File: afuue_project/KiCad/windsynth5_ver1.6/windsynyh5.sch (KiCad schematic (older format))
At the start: 29 parts, among them P1 SENSOR, P2 SPEAKER, P3 HEADPHONE, P4 POWER, P5 EXT, P6 AE-PAM8012, P7 I2C, P8 TRS MIDI, SW1 SW_SPDT, U1 ESP32-DEVKIT-C, U2 L7805

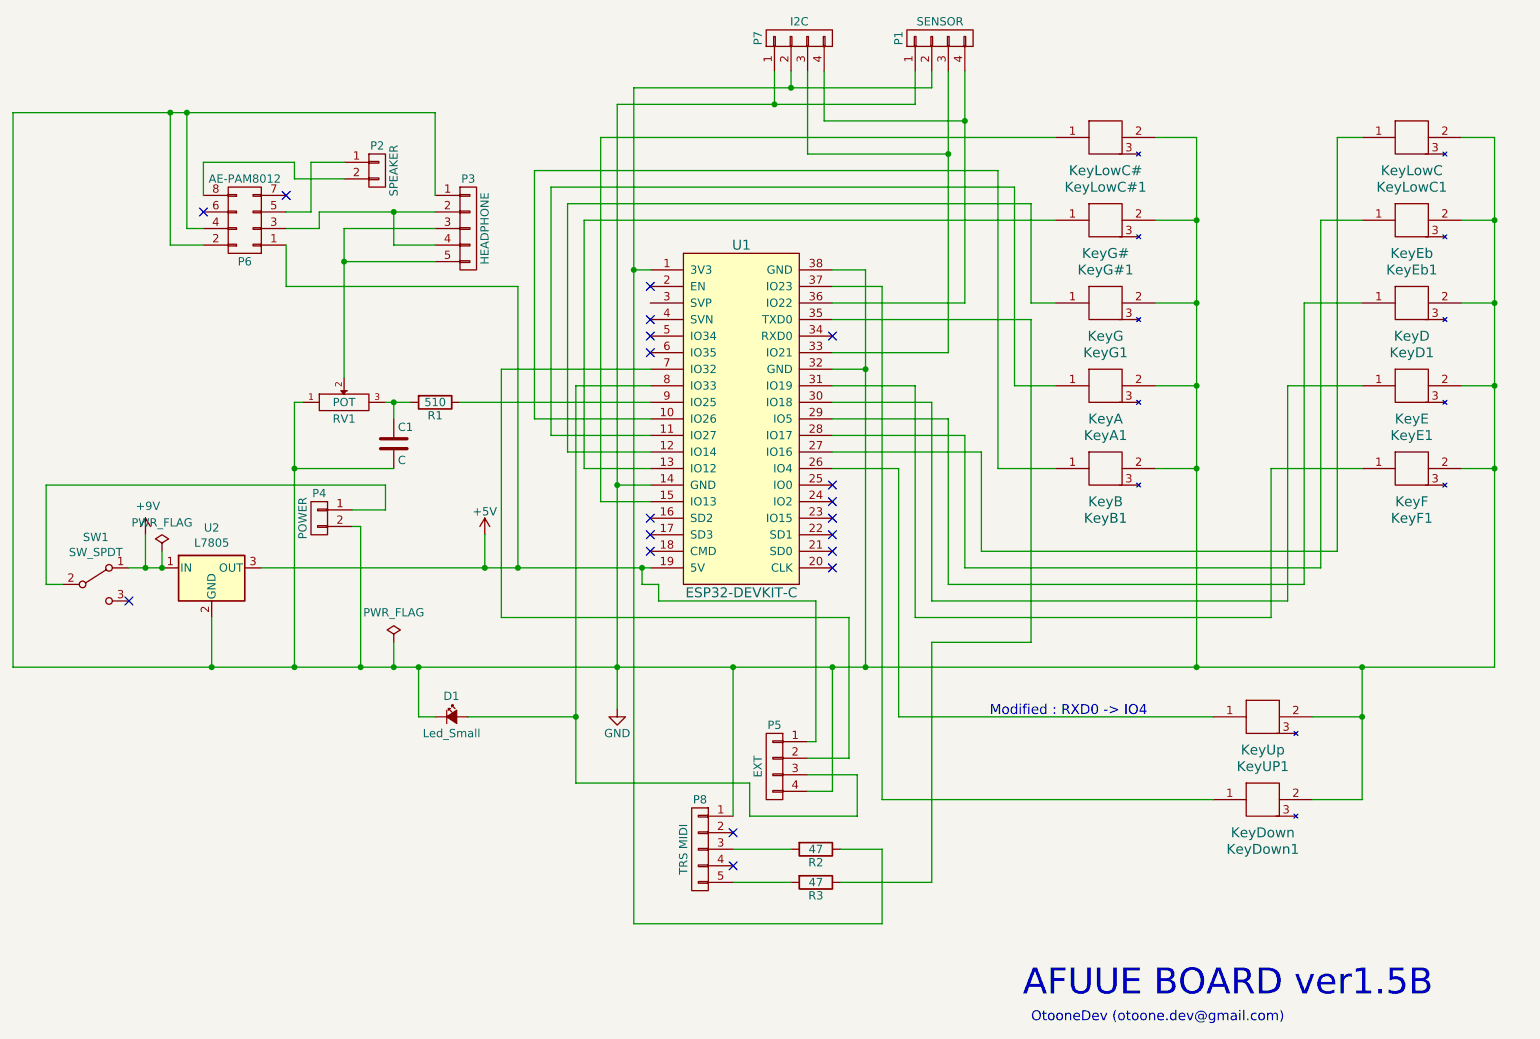
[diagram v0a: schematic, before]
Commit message: 電池内蔵版v06のソースやデータを追加
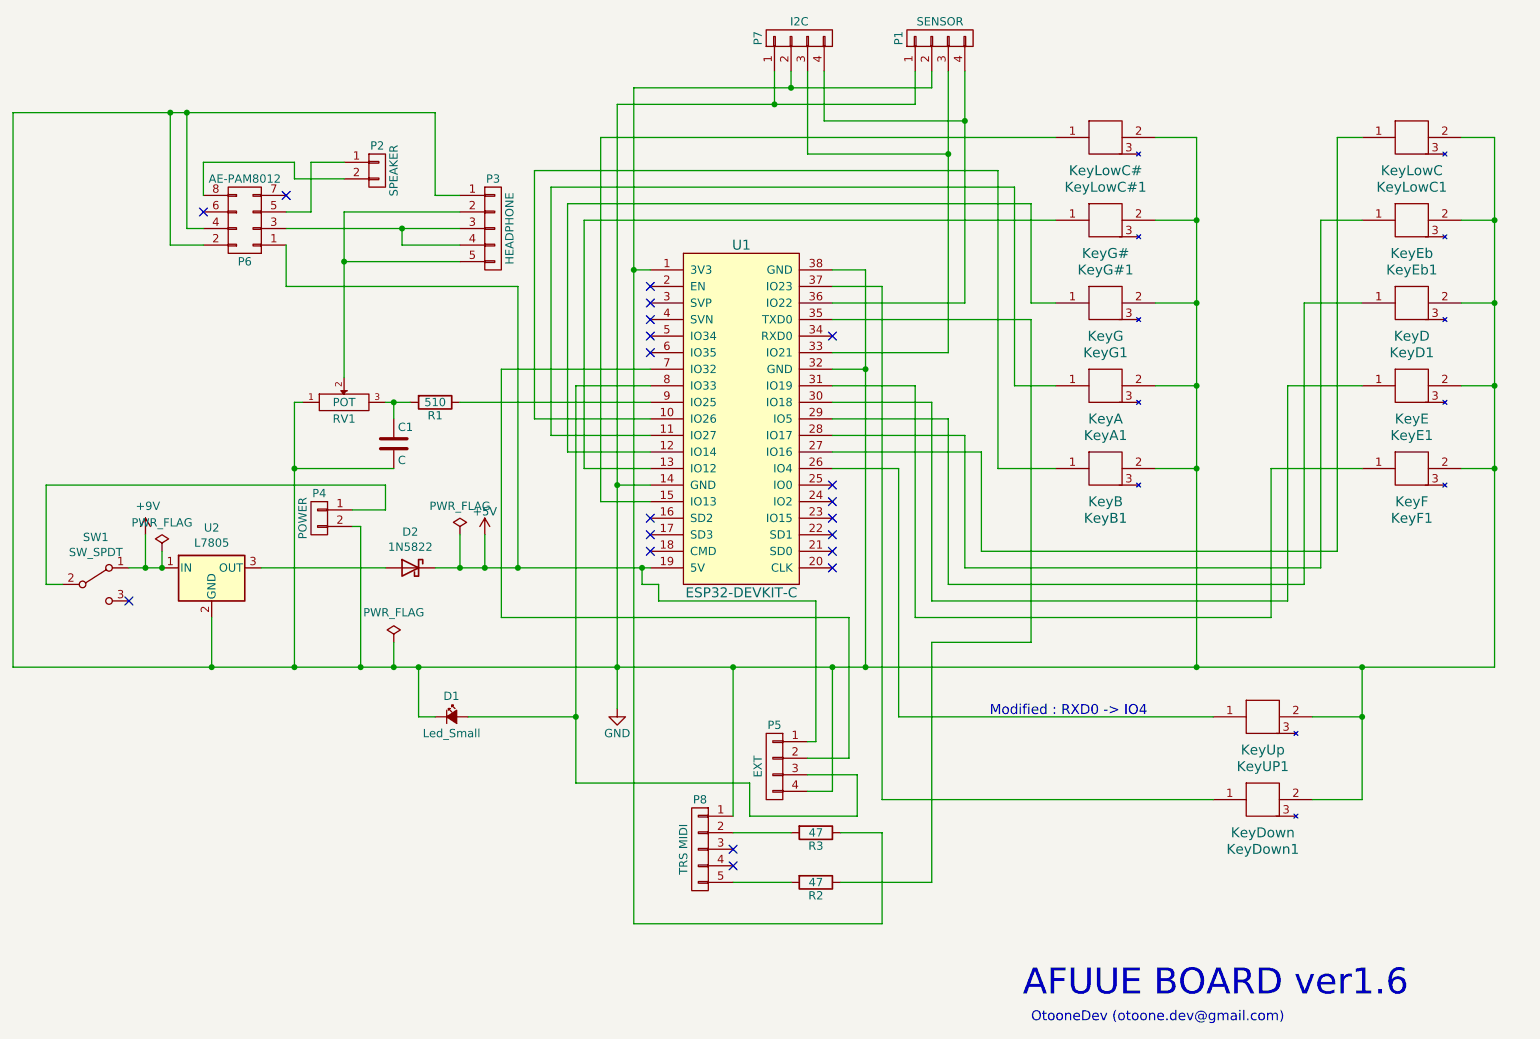
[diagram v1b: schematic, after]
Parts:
- added D2: 1N5822, Connector_PinHeader_2.54mm:PinHeader_1x02_P2.54mm_Vertical, symbol Diode:1N5822
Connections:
- net +5V: now also D2.1 (K); no longer U2.3 (OUT)
- net at P1.2 (P2), P7.2 (P2), U1.1 (3V3): now also R3.1; no longer R2.1
- net at U1.35 (TXD0): now also R2.1; no longer R3.1
- net at P3.5 (P5), RV1.2: now also P3.2 (P2); no longer P3.3 (P3)
- net at P3.4 (P4), P6.3 (P3): now also P3.3 (P3); no longer P3.2 (P2)
- net at P8.2 (P2): now also R3.2
- net at P8.3 (P3): no longer R2.2
- net at P8.5 (P5): now also R2.2; no longer R3.2
- new net: D2.2 (A), U2.3 (OUT)
- no-connect marks 19 -> 20
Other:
- note added: "AFUUE BOARD ver1.6"
- note removed: "AFUUE BOARD ver1.5B"
- moved on the sheet: P3, R2, R3
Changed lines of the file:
@@
 L windsynyh5-rescue:CONN_01X05 P3
 U 1 1 5E29EC6C
-P 3800 2200
-F 0 "P3" H 3800 2500 50  0000 C CNN
-F 1 "HEADPHONE" V 3900 2200 50  0000 C CNN
-F 2 "HPJack_PJ307:PJ-307 AudioJack" H 3800 2200 50  0001 C CNN
-F 3 "" H 3800 2200 50  0000 C CNN
-	1    3800 2200
+P 3950 2200
+F 0 "P3" H 3950 2500 50  0000 C CNN
+F 1 "HEADPHONE" V 4050 2200 50  0000 C CNN
+F 2 "HPJack_PJ307:PJ-307 AudioJack" H 3950 2200 50  0001 C CNN
+F 3 "" H 3950 2200 50  0000 C CNN
+	1    3950 2200
 	1    0    0    -1
 $EndComp
@@
 NoConn ~ 2200 2100
 Text Notes 7150 6850 0    157  ~ 0
-AFUUE BOARD ver1.5B
+AFUUE BOARD ver1.6
 Text Notes 7200 7000 0    60   ~ 0
 OtooneDev (otoone.dev@gmail.com)
@@
 L Device:R R3
 U 1 1 5F3D1BEC
+P 5900 5850
+F 0 "R3" V 5980 5850 50  0000 C CNN
+F 1 "47" V 5900 5850 50  0000 C CNN
+F 2 "Pin_Headers:Pin_Header_Straight_1x02_Pitch2.54mm" V 5830 5850 50  0001 C CNN
+F 3 "" H 5900 5850 50  0000 C CNN
+	1    5900 5850
+	0    1    1    0
+$EndComp
+$Comp
+L Device:R R2
+U 1 1 5F3D23AC
 P 5900 6150
-F 0 "R3" V 5980 6150 50  0000 C CNN
+F 0 "R2" V 5980 6150 50  0000 C CNN
 F 1 "47" V 5900 6150 50  0000 C CNN
 F 2 "Pin_Headers:Pin_Header_Straight_1x02_Pitch2.54mm" V 5830 6150 50  0001 C CNN
@@
 	0    1    1    0
 $EndComp
-$Comp
-L Device:R R2
-U 1 1 5F3D23AC
-P 5900 5950
-F 0 "R2" V 5980 5950 50  0000 C CNN
-F 1 "47" V 5900 5950 50  0000 C CNN
-F 2 "Pin_Headers:Pin_Header_Straight_1x02_Pitch2.54mm" V 5830 5950 50  0001 C CNN
-F 3 "" H 5900 5950 50  0000 C CNN
-	1    5900 5950
-	0    1    1    0
-$EndComp
-NoConn ~ 5400 5850
 NoConn ~ 5400 6050
 NoConn ~ 6000 4050
@@
 	0    1    1    0
 $EndComp
-$Comp
-L windsynyh5-rescue:Led_Small D1
-U 1 1 5F3D4A68
-P 3700 5150
-F 0 "D1" H 3650 5275 50  0000 L CNN
-F 1 "Led_Small" H 3525 5050 50  0000 L CNN
-F 2 "Pin_Headers:Pin_Header_Straight_1x02_Pitch2.54mm" V 3700 5150 50  0001 C CNN
-F 3 "" V 3700 5150 50  0000 C CNN
-	1    3700 5150
-	1    0    0    -1
-$EndComp
 NoConn ~ 4900 4050
 NoConn ~ 4900 2850
@@
 Connection ~ 3350 4850
 Wire Wire Line
-	3050 2400 3600 2400
-Wire Wire Line
 	3600 1500 3600 2000
 Wire Wire Line
@@
 Wire Wire Line
 	7200 4700 6600 4700
-Wire Wire Line
-	6600 4700 6600 6150
-Wire Wire Line
-	3050 2200 3050 2400
 Wire Wire Line
 	2700 2100 2850 2100
@@
 Wire Wire Line
 	4950 4450 5900 4450
-Connection ~ 3900 4250
 Wire Wire Line
 	3300 3900 3100 3900
@@
 	5400 6150 5750 6150
 Connection ~ 4800 2450
-Wire Wire Line
-	3600 2200 3050 2200
 Connection ~ 3050 2400
-Wire Wire Line
-	2900 2100 3350 2100
-Wire Wire Line
-	2900 2100 2900 2200
-Wire Wire Line
-	2900 2200 2700 2200
-Wire Wire Line
-	3600 2300 3350 2300
-Wire Wire Line
-	3350 2300 3350 2100
-Connection ~ 3350 2100
-Wire Wire Line
-	5400 5950 5750 5950
 Wire Wire Line
 	4100 2550 2700 2550
@@
 Connection ~ 3500 4850
 Wire Wire Line
-	3800 5150 4450 5150
-Wire Wire Line
 	4450 5550 5500 5550
-Connection ~ 4450 5150
 Wire Wire Line
 	6000 3650 6400 3650
 Wire Wire Line
 	6150 5500 5850 5500
-Wire Wire Line
-	4450 3150 4450 5150
-Wire Wire Line
-	6600 6150 6050 6150
-Wire Wire Line
-	6050 5950 6300 5950
-Wire Wire Line
-	6300 5950 6300 6400
 Wire Wire Line
 	6300 6400 4800 6400
@@
 	3050 2400 3050 3100
 Wire Wire Line
-	3350 2100 3600 2100
-Wire Wire Line
 	6200 3050 6200 4850
 Wire Wire Line
 	3500 4850 3350 4850
-Wire Wire Line
-	4450 5150 4450 5550
 Wire Wire Line
 	3150 4850 2750 4850
@@
 	1950 4150 1950 4250
 Connection ~ 1950 4250
-Wire Wire Line
-	2550 4250 3900 4250
 $Comp
 L Switch:SW_SPDT SW1
@@
 	1    0    0    -1
 $EndComp
+Wire Wire Line
+	3750 2100 3050 2100
+Wire Wire Line
+	3050 2100 3050 2400
+Wire Wire Line
+	3050 2400 3750 2400
+Wire Wire Line
+	2700 2200 3400 2200
+Wire Wire Line
+	3750 2300 3400 2300
+Wire Wire Line
+	3400 2300 3400 2200
+Connection ~ 3400 2200
+Wire Wire Line
+	3400 2200 3750 2200
+Wire Wire Line
+	3600 2000 3750 2000
+Wire Wire Line
+	6600 4700 6600 6150
+Wire Wire Line
+	6600 6150 6050 6150
+Wire Wire Line
+	6300 6400 6300 5850
+Wire Wire Line
+	6300 5850 6050 5850
+Wire Wire Line
+	5750 5850 5400 5850
+NoConn ~ 5400 5950
+$Comp
+L Diode:1N5822 D2
+U 1 1 6026CD17
+P 3450 4250
+F 0 "D2" H 3450 4467 50  0000 C CNN
+F 1 "1N5822" H 3450 4376 50  0000 C CNN
+F 2 "Connector_PinHeader_2.54mm:PinHeader_1x02_P2.54mm_Vertical" H 3450 4075 50  0001 C CNN
+F 3 "http://www.vishay.com/docs/88526/1n5820.pdf" H 3450 4250 50  0001 C CNN
+	1    3450 4250
+	-1   0    0    -1
+$EndComp
+Wire Wire Line
+	3900 4250 3750 4250
+Connection ~ 3900 4250
+Wire Wire Line
+	3300 4250 2550 4250
+Wire Wire Line
+	4450 3150 4450 5150
+Connection ~ 4450 5150
+Wire Wire Line
+	4450 5150 4450 5550
+Wire Wire Line
+	3800 5150 4450 5150
+$Comp
+L windsynyh5-rescue:Led_Small D1
+U 1 1 5F3D4A68
+P 3700 5150
+F 0 "D1" H 3650 5275 50  0000 L CNN
+F 1 "Led_Small" H 3525 5050 50  0000 L CNN
+F 2 "Pin_Headers:Pin_Header_Straight_1x02_Pitch2.54mm" V 3700 5150 50  0001 C CNN
+F 3 "" V 3700 5150 50  0000 C CNN
+	1    3700 5150
+	1    0    0    -1
+$EndComp
+$Comp
+L power:PWR_FLAG #FLG0102
+U 1 1 60297D7D
+P 3750 4050
+F 0 "#FLG0102" H 3750 4125 50  0001 C CNN
+F 1 "PWR_FLAG" H 3750 4223 50  0000 C CNN
+F 2 "" H 3750 4050 50  0001 C CNN
+F 3 "~" H 3750 4050 50  0001 C CNN
+	1    3750 4050
+	1    0    0    -1
+$EndComp
+Wire Wire Line
+	3750 4050 3750 4250
+Connection ~ 3750 4250
+Wire Wire Line
+	3750 4250 3600 4250
+NoConn ~ 4900 2650
 $EndSCHEMATC

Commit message: v6向け更新
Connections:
- net at P1.2 (P2), P7.2 (P2), U1.1 (3V3): now also R2.1; no longer R3.1
- net at U1.35 (TXD0): now also R3.1; no longer R2.1
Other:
- note added: "AFUUE BOARD ver1.6C"
- note removed: "AFUUE BOARD ver1.6"
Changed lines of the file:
@@
 NoConn ~ 2200 2100
 Text Notes 7150 6850 0    157  ~ 0
-AFUUE BOARD ver1.6
+AFUUE BOARD ver1.6C
 Text Notes 7200 7000 0    60   ~ 0
 OtooneDev (otoone.dev@gmail.com)
@@
 	3600 2000 3750 2000
 Wire Wire Line
-	6600 4700 6600 6150
-Wire Wire Line
-	6600 6150 6050 6150
-Wire Wire Line
-	6300 6400 6300 5850
-Wire Wire Line
-	6300 5850 6050 5850
-Wire Wire Line
 	5750 5850 5400 5850
 NoConn ~ 5400 5950
@@
 	3750 4250 3600 4250
 NoConn ~ 4900 2650
+Wire Wire Line
+	6600 4700 6600 5850
+Wire Wire Line
+	6050 5850 6600 5850
+Wire Wire Line
+	6300 6400 6300 6150
+Wire Wire Line
+	6300 6150 6050 6150
 $EndSCHEMATC
